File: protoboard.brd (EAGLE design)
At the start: 63.2 x 61 mm, 2 parts

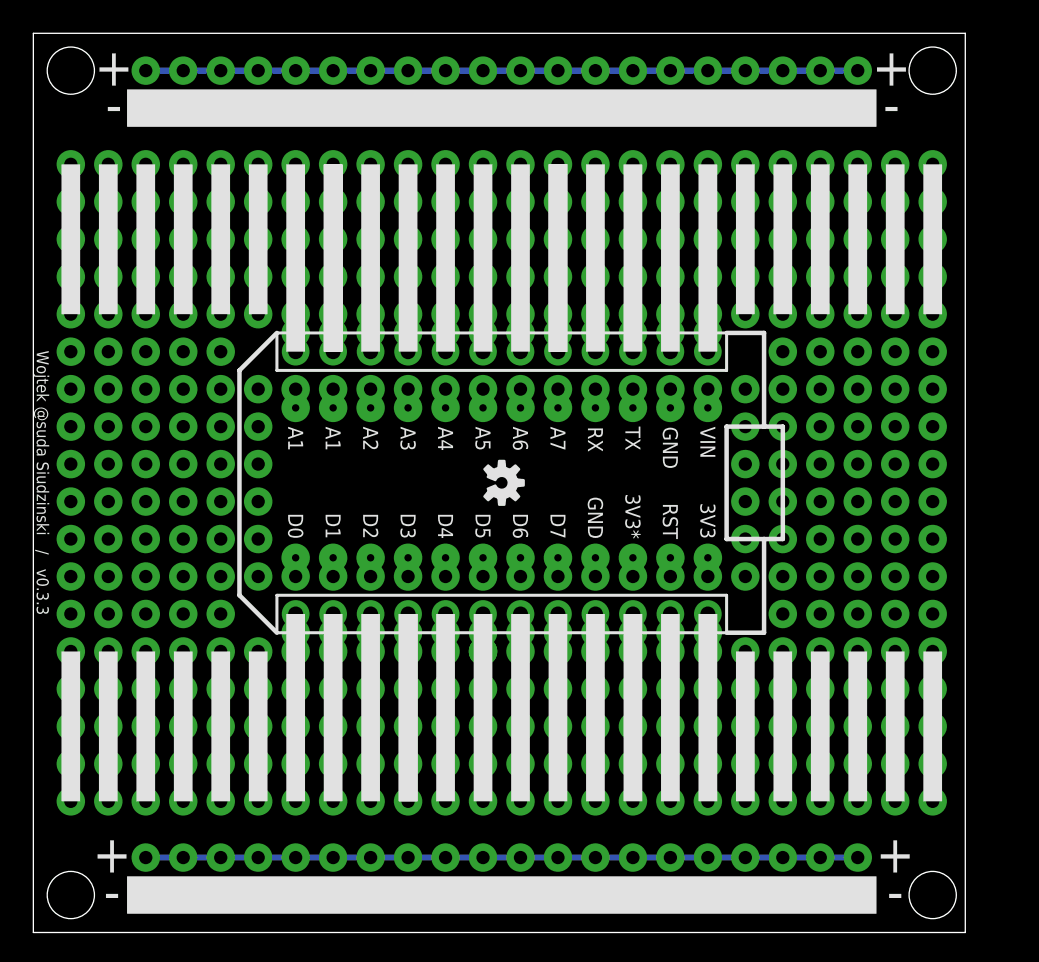
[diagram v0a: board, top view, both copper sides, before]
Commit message: Moved Core/Photon to the side
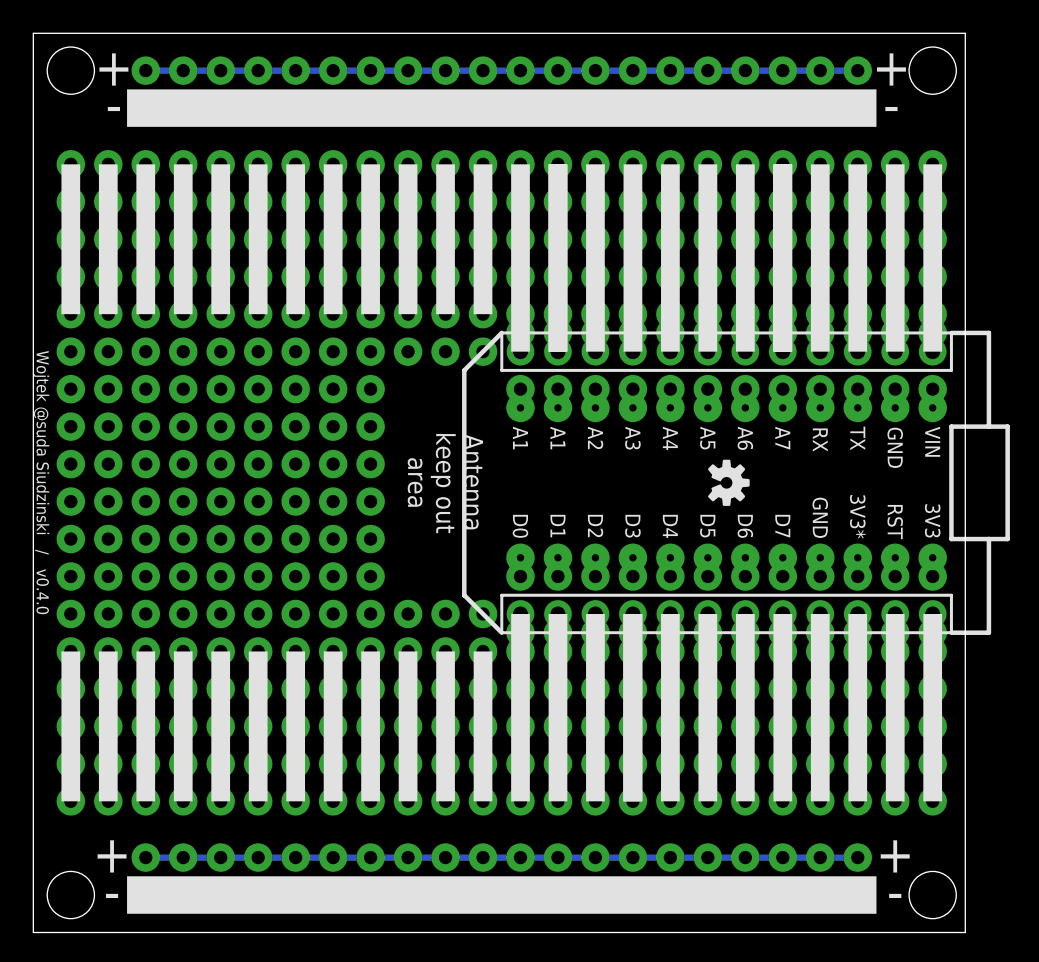
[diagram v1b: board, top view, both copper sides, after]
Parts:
- moved CORE/PHOTON 15.2 mm to (47.0, 49.5)
- moved E$1 15.2 mm to (47.0, 49.5)
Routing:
- net S$43: track 478.8 -> 10.2 mm, vias 240 -> 5
- net S$54: track 0.00 -> 10.2 mm
- net S$3: track 0.00 -> 10.2 mm, vias 0 -> 4
- net S$185: track 0.00 -> 10.2 mm, vias 0 -> 4
- net S$171: track 0.00 -> 10.2 mm, vias 0 -> 5
- net S$170: track 0.00 -> 10.2 mm, vias 0 -> 5
- net S$169: track 0.00 -> 10.2 mm, vias 0 -> 5
- net S$167: track 0.00 -> 10.2 mm, vias 0 -> 5
- net S$166: track 0.00 -> 10.2 mm, vias 0 -> 5
- net S$130: track 0.00 -> 10.2 mm, vias 0 -> 5
- net S$129: track 0.00 -> 10.2 mm, vias 0 -> 5
- net S$126: track 0.00 -> 10.2 mm, vias 0 -> 5
- net S$125: track 0.00 -> 10.2 mm, vias 0 -> 5
- net S$124: track 0.00 -> 10.2 mm, vias 0 -> 5
- net S$123: track 0.00 -> 10.2 mm, vias 0 -> 5
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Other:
- board text added: "Antenna keep out area"
- board text added: "Wojtek @suda Siudzinski / v0.4.0"
- board text removed: "Wojtek @suda Siudzinski / v0.3.3"
